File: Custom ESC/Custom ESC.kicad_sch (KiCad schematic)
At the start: 55 parts, among them J2 Conn_ARM_SWD_TagConnect_TC203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, Q1 NMOS, Q2 NMOS, Q3 NMOS, Q4 NMOS, Q5 NMOS, Q6 NMOS, SW1 SW_Push, SW2 SW_SPDT, U1 STM32G4A1CETx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

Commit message: Did CurrentSense
Implemented CurrentSense schematic using the IR2133S gate driver's internal current sense amplifier. Need to implement Back EMF and then layouts!
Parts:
- added R12, R13, R14, R15, R16: 10k, Resistor_SMD:R_0603_1608Metric_Pad0.98x0.95mm_HandSolder, symbol Device:R
- R11: value R_Shunt -> 1m; footprint (none) -> Resistor_SMD:R_Shunt_Vishay_WSR2_WSR3_KelvinConnection
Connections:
- net COM: now also Q2.3 (S), Q4.3 (S), Q6.3 (S)
- net GND: now also R11.2, R13.1, R16.1
- net at R11.3: now also R14.2, R15.2
- net ITRIP: now reaches U4.1 (ITRIP)
- net ITRIP: now also R15.1, R16.2
- net CAO: now reaches U4.3 (CAO)
- net CAO: now also R12.2
- net CA-: now reaches U4.4 (CA-)
- net CA-: now also R12.1, R13.2
- net CA+: now reaches U4.5 (CA+)
- net CA+: now also R14.1
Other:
- moved on the sheet: C21, C22, C24, C25, C26, D2, D3, D4

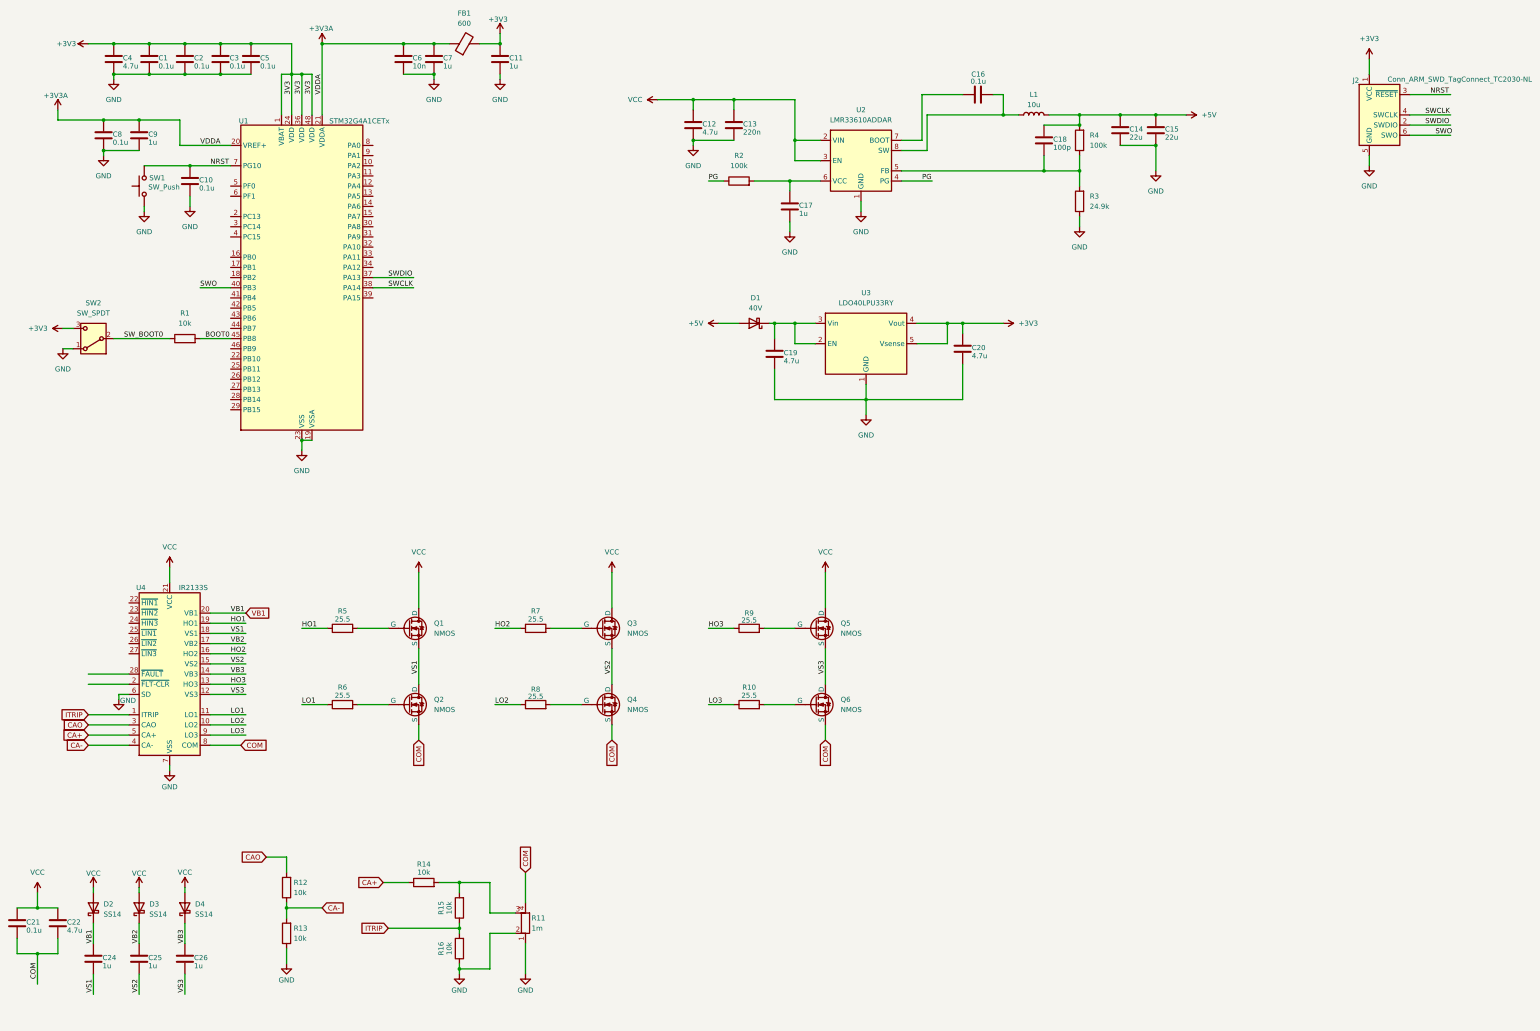
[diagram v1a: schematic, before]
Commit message: Fixed up some minor schematic details
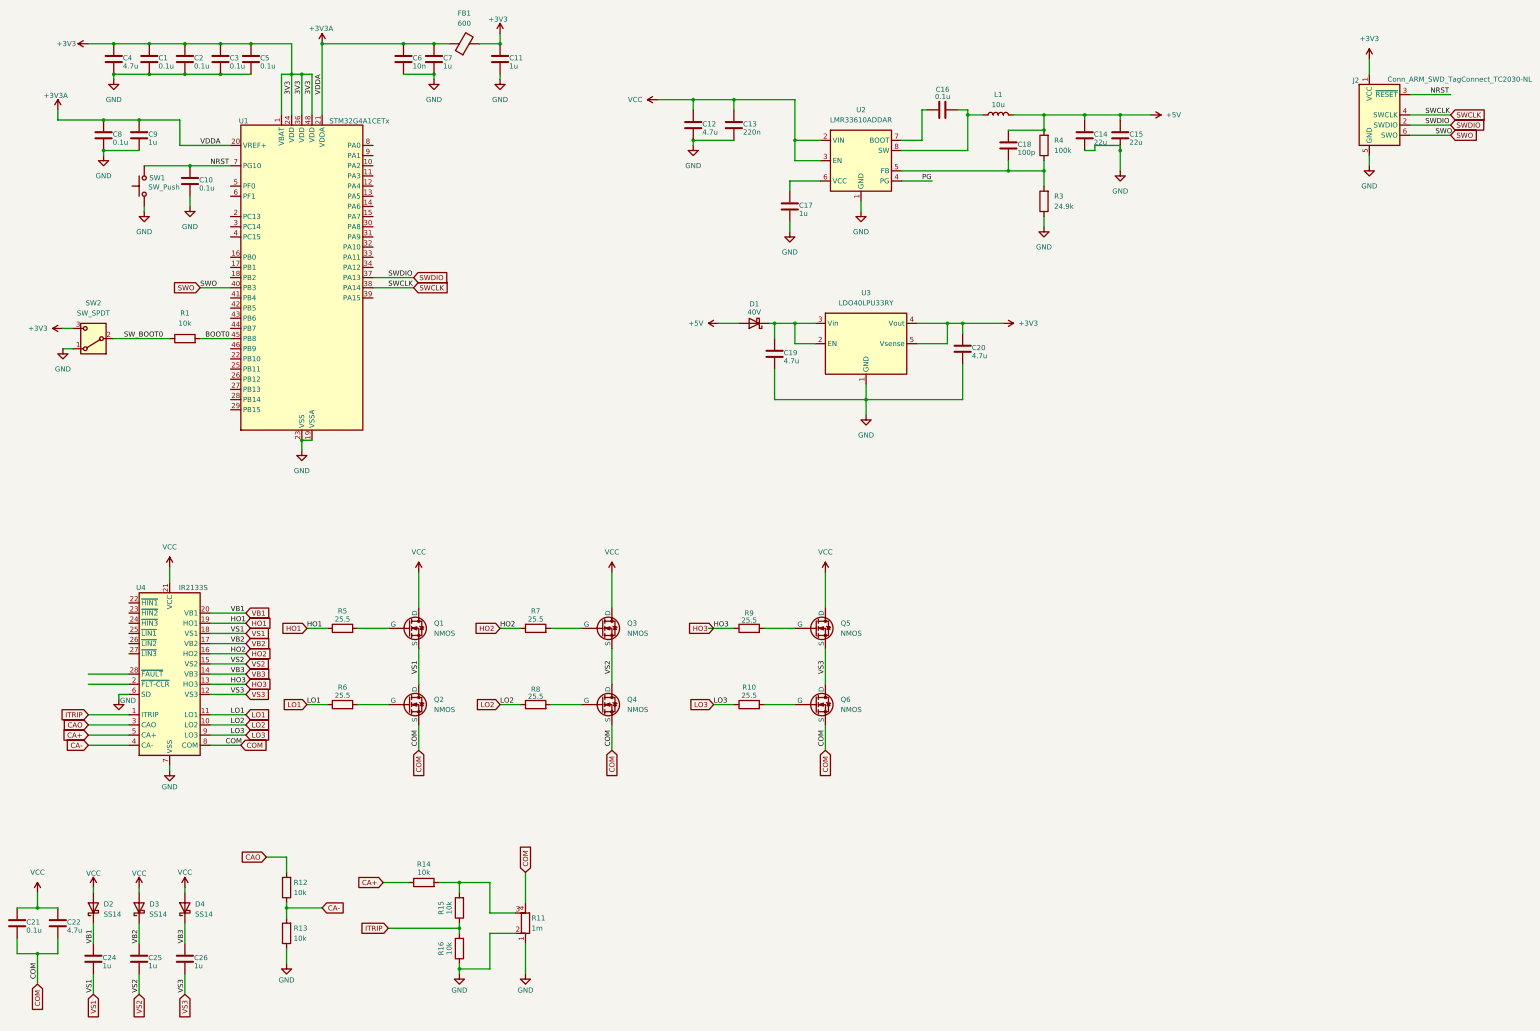
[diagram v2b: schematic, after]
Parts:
- removed R2: 100k, Resistor_SMD:R_0603_1608Metric_Pad0.98x0.95mm_HandSolder, symbol Device:R
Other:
- moved on the sheet: C14, C15, C16, C18, L1, R3, R4
